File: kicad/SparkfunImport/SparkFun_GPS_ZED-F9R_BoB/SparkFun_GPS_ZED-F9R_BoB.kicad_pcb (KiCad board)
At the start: 2 copper layers, 43.2 x 50.8 mm, 145 parts, among them J1 U.FL, J2 USB_C_2-LAYER_PADS, J3 QWIIC_RIGHT_ANGLE, J4 QWIIC_RIGHT_ANGLE, J5 CONN_111X11_NO_SILK, J6 CONN_09NO_SILK, J7 CONN_06NO_SILK_NO_POP, U1 DUAL-OPTO_HCPL-073L, U2 U-BLOX_ZED_F9R, U3 UHS_INVERTER_SCHMITT_TRIGGERS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

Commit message: Starting to make gps_breakout
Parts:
- moved BT1 149.8 mm to (29.1, 7.49)
- moved C1 149.8 mm to (27.6, 45.1)
- moved C10 149.8 mm to (26.2, 12.7)
- moved C2 149.8 mm to (25.4, 15.9)
- moved C3 149.8 mm to (36.0, 32.8)
- moved C4 149.8 mm to (35.6, 43.9)
- moved C5 149.8 mm to (19.8, 16.0)
- moved C6 149.8 mm to (26.2, 37.4)
- moved C8 149.8 mm to (21.1, 37.0)
- moved D1 149.8 mm to (36.0, 35.3)
- moved D2 149.8 mm to (36.1, 41.5)
- moved D3 149.8 mm to (12.4, 8.84)
- moved D4 149.8 mm to (24.1, 48.3)
- moved D5 149.8 mm to (28.4, 48.3)
- moved D6 149.8 mm to (35.9, 48.3)
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
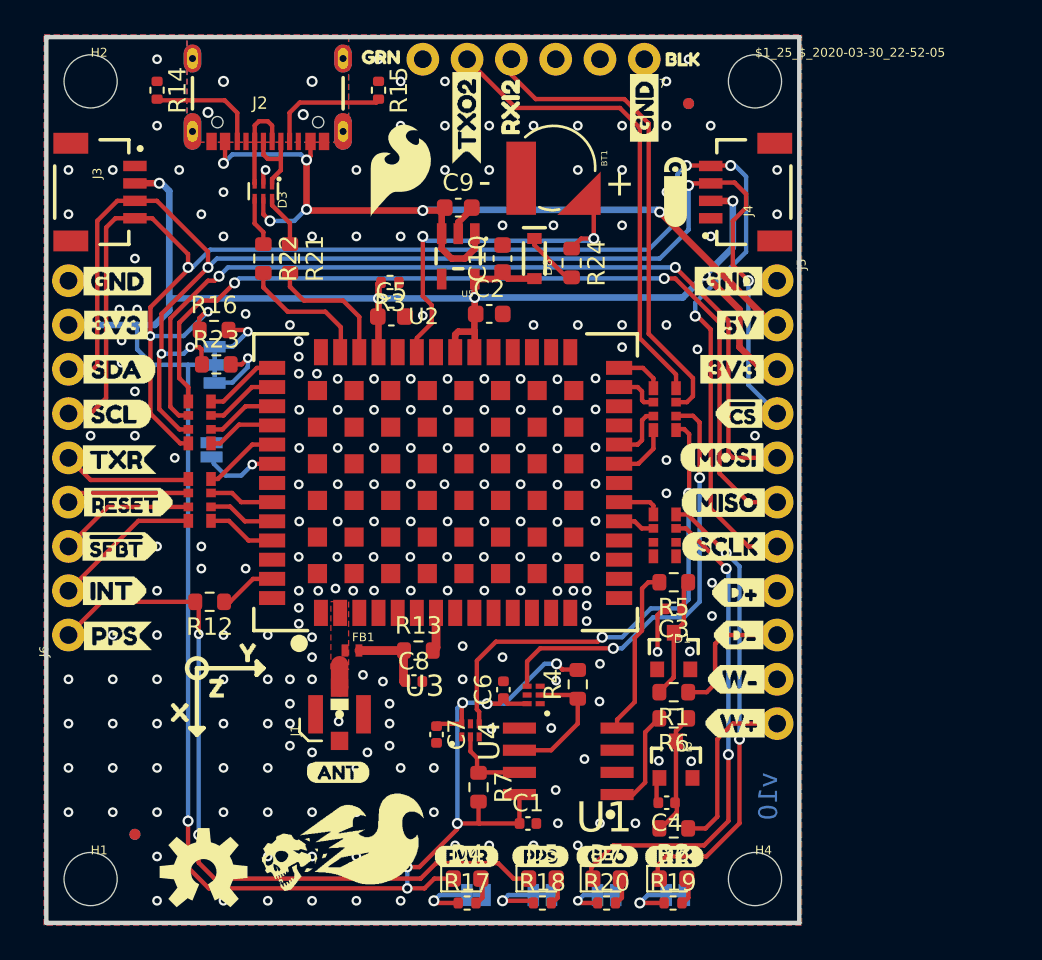
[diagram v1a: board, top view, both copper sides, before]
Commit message: Added BME280 and ICM20948 stamps
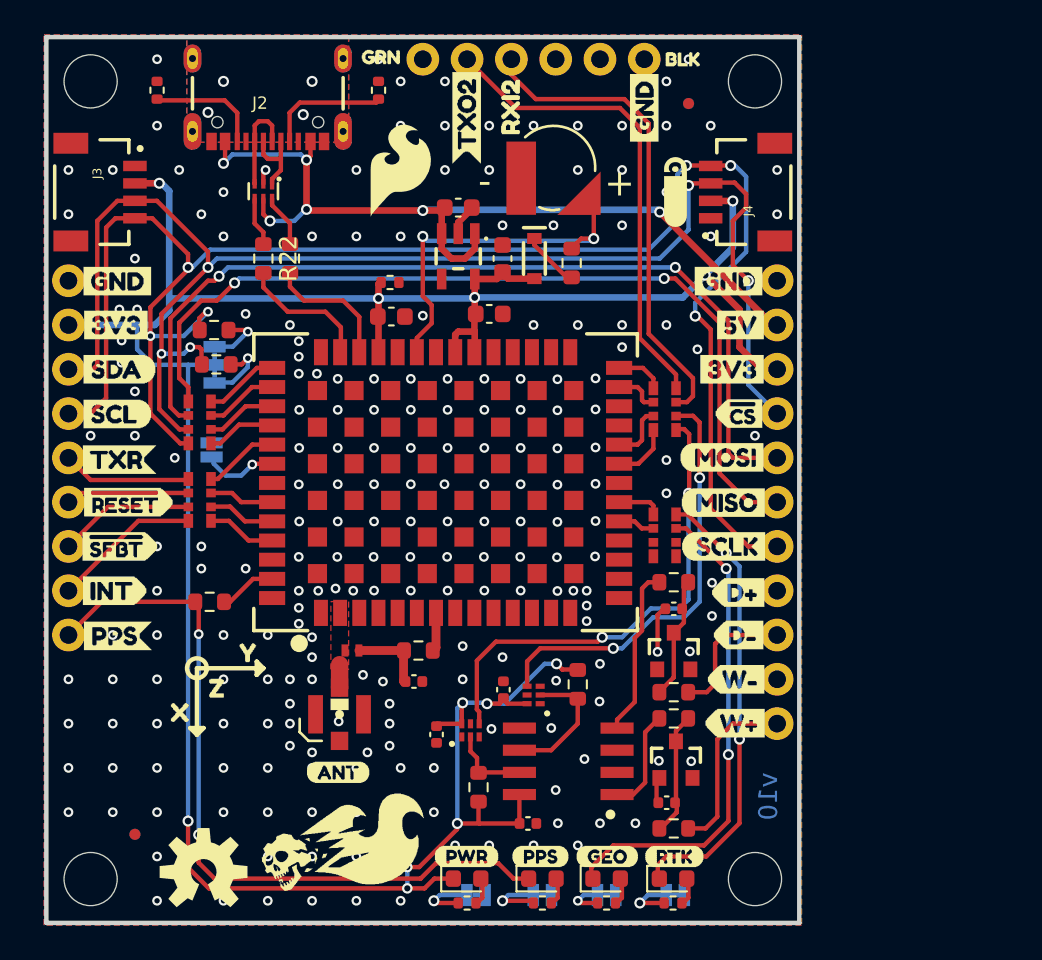
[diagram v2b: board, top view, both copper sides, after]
